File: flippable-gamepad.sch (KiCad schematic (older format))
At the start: 24 parts, among them SW1 SW_Push, U1 ATmega32U4-AU, Y1 16MHz

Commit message: Add ProMicro footprints
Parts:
- added ProMicro1: ProMicro, symbol promicro:ProMicro
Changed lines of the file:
@@
 Text GLabel 8450 3750 1    50   Input ~ 0
 COL1
+$Comp
+L promicro:ProMicro ProMicro1
+U 1 1 616FA80C
+P 6450 1900
+F 0 "ProMicro1" H 6450 2937 60  0000 C CNN
+F 1 "ProMicro" H 6450 2831 60  0000 C CNN
+F 2 "" H 6550 850 60  0000 C CNN
+F 3 "" H 6550 850 60  0000 C CNN
+	1    6450 1900
+	1    0    0    -1
+$EndComp
 $EndSCHEMATC

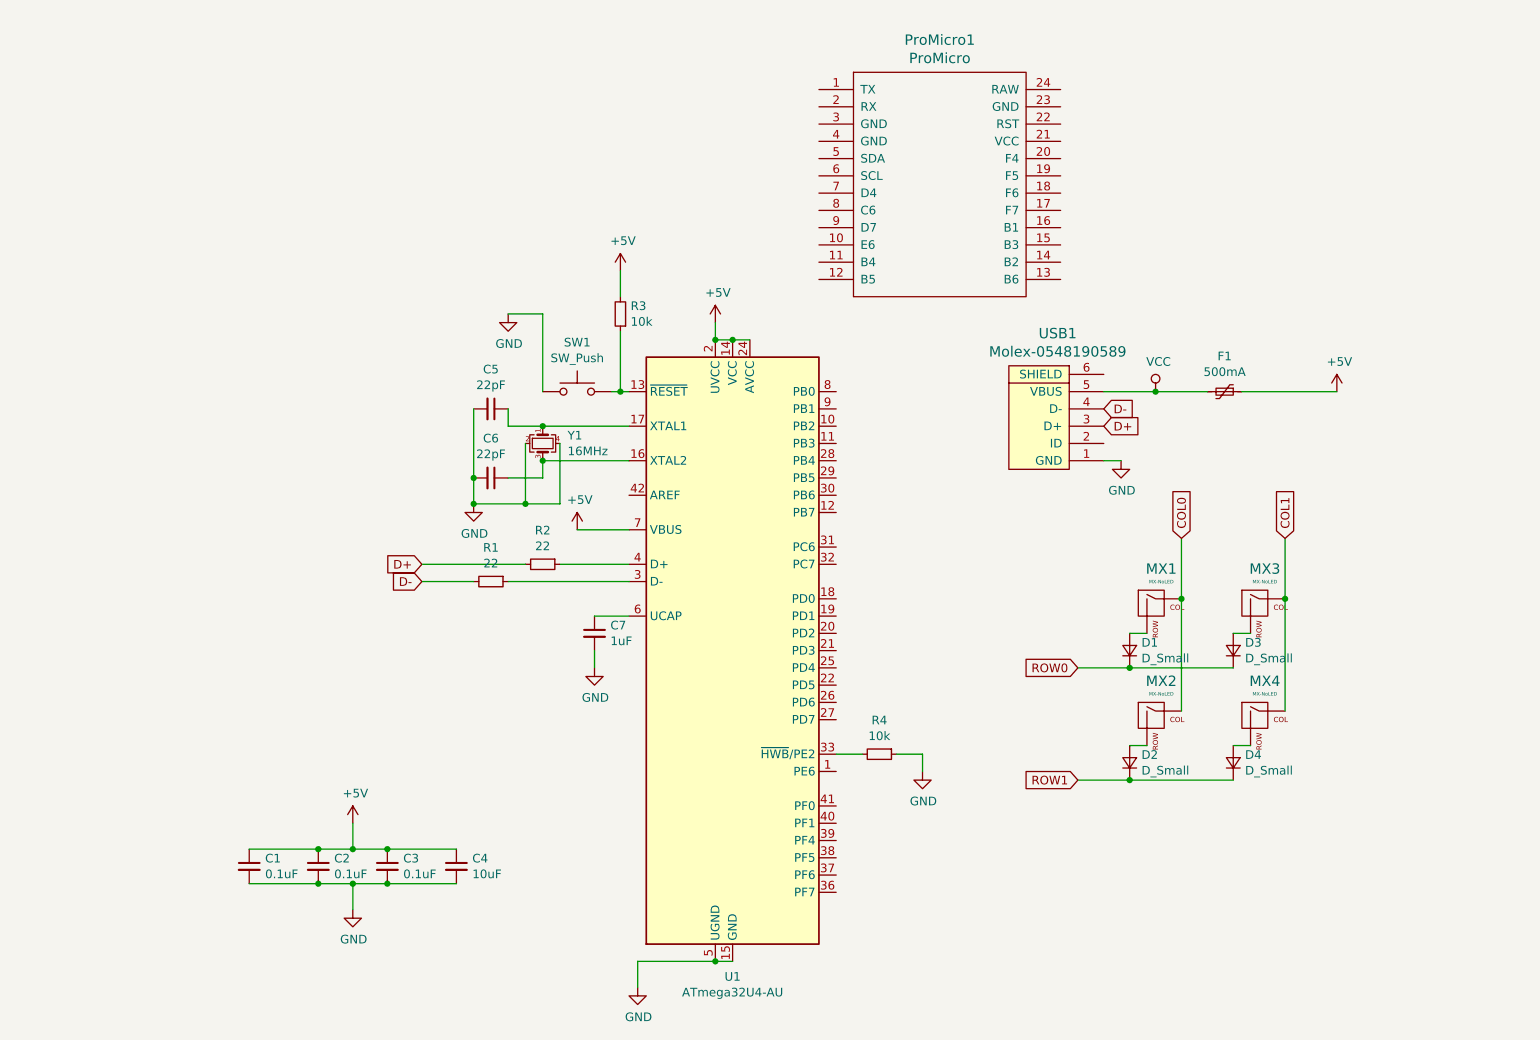
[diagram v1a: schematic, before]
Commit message: Non flippable version test
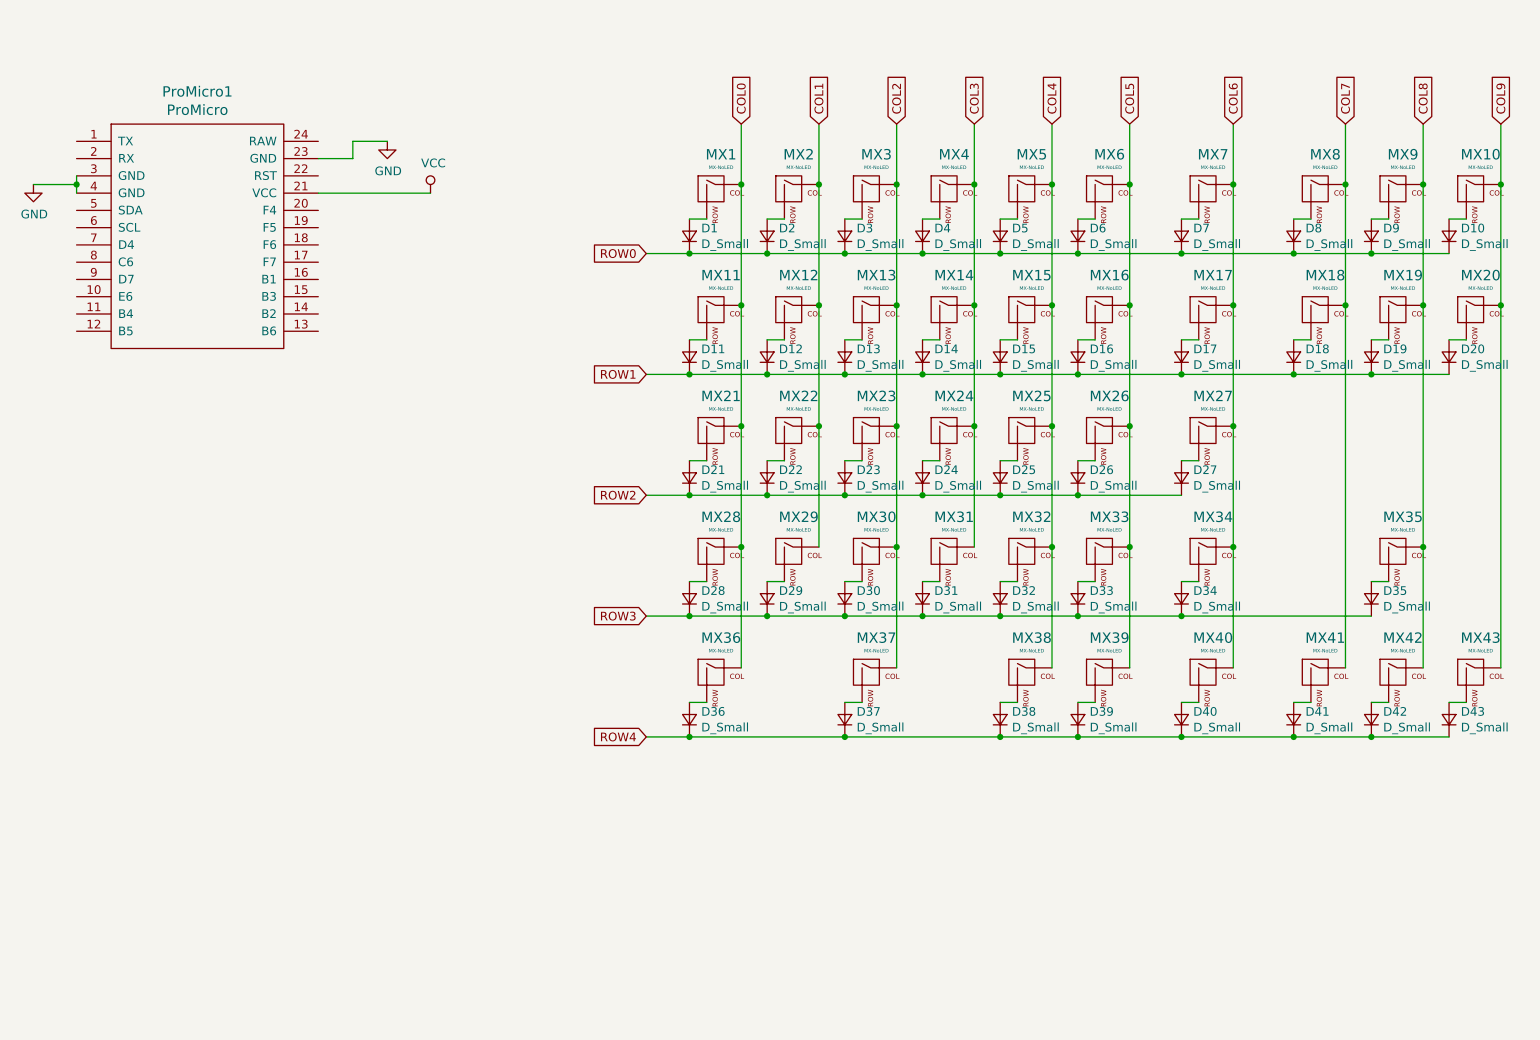
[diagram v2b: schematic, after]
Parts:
- removed C1, C2, C3: 0.1uF, Capacitor_SMD:C_0805_2012Metric, symbol Device:C_Small
- removed C4: 10uF, Capacitor_SMD:C_0805_2012Metric, symbol Device:C_Small
- removed C5, C6: 22pF, Capacitor_SMD:C_0805_2012Metric, symbol Device:C_Small
- removed C7: 1uF, Capacitor_SMD:C_0805_2012Metric, symbol Device:C_Small
- removed F1: 500mA, Fuse:Fuse_1206_3216Metric, symbol Device:Polyfuse_Small
- removed R1, R2: 22, Resistor_SMD:R_0805_2012Metric, symbol Device:R_Small
- removed R3, R4: 10k, Resistor_SMD:R_0805_2012Metric, symbol Device:R_Small
- removed SW1: SW_Push, random-keyboard-parts:SKQG-1155865, symbol Switch:SW_Push
- removed U1: ATmega32U4-AU, Package_QFP:TQFP-44_10x10mm_P0.8mm, symbol MCU_Microchip_ATmega:ATmega32U4-AU
- removed USB1: Molex-0548190589, random-keyboard-parts:Molex-0548190589, symbol random-keyboard-parts:Molex-0548190589
- removed Y1: 16MHz, Crystal:Crystal_SMD_3225-4Pin_3.2x2.5mm, symbol Device:Crystal_GND24_Small
- added D10, D11, D12, D13, D14, D15, D16, D17, D18, D19, D20, D21, D22, D23, D24, D25, D26, D27, D28, D29, D30, D31, D32, D33, D34, D35, D36, D37, D38, D39, D40, D41, D42, D43, D5, D6, D7, D8, D9: D_Small, Diode_SMD:D_SOD-123, symbol Device:D_Small
- added MX10, MX11, MX12, MX13, MX14, MX15, MX16, MX18, MX19, MX20, MX21, MX22, MX23, MX24, MX25, MX26, MX28, MX29, MX30, MX31, MX32, MX33, MX35, MX36, MX38, MX39, MX41, MX42, MX43, MX5, MX6, MX8, MX9: MX-NoLED, MX_Only:MXOnly-1U-NoLED, symbol MX_Alps_Hybrid:MX-NoLED
- added MX17, MX27, MX34, MX40, MX7: MX-NoLED, MX_Only:MXOnly-1.25U-NoLED, symbol MX_Alps_Hybrid:MX-NoLED
- added MX37: MX-NoLED, MX_Only:MXOnly-3U-NoLED, symbol MX_Alps_Hybrid:MX-NoLED
- ProMicro1: footprint (none) -> promicro:ProMicro
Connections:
- net COL0: now also MX11.1 (COL), MX21.1 (COL), MX28.1 (COL), MX36.1 (COL); no longer MX2.1 (COL)
- net COL1: now also MX2.1 (COL), MX12.1 (COL), MX22.1 (COL), MX29.1 (COL); no longer MX3.1 (COL), MX4.1 (COL)
- net GND: now also ProMicro1.23 (GND), ProMicro1.3 (GND), ProMicro1.4 (GND)
- net ROW0: now also D2.1 (K), D4.1 (K), D10.1 (K), D5.1 (K), D6.1 (K), D7.1 (K), D8.1 (K), D9.1 (K)
- net ROW1: now also D11.1 (K), D12.1 (K), D13.1 (K), D14.1 (K), D15.1 (K), D16.1 (K), D17.1 (K), D18.1 (K), D19.1 (K), D20.1 (K); no longer D2.1 (K), D4.1 (K)
- net VCC: now also ProMicro1.21 (VCC)
- new net: D5.2 (A), MX5.2 (ROW)
- new net: D6.2 (A), MX6.2 (ROW)
- new net: D11.2 (A), MX11.2 (ROW)
- new net: D12.2 (A), MX12.2 (ROW)
- new net: D13.2 (A), MX13.2 (ROW)
- new net: D14.2 (A), MX14.2 (ROW)
- new net: D15.2 (A), MX15.2 (ROW)
- new net: D16.2 (A), MX16.2 (ROW)
- new net: D21.2 (A), MX21.2 (ROW)
- new net: D22.2 (A), MX22.2 (ROW)
- new net: D23.2 (A), MX23.2 (ROW)
- new net: D24.2 (A), MX24.2 (ROW)
- new net: D25.2 (A), MX25.2 (ROW)
- new net: D26.2 (A), MX26.2 (ROW)
- new net: D28.2 (A), MX28.2 (ROW)
- new net: D29.2 (A), MX29.2 (ROW)
- new net: D30.2 (A), MX30.2 (ROW)
- new net: D31.2 (A), MX31.2 (ROW)
- new net: D32.2 (A), MX32.2 (ROW)
- new net: D33.2 (A), MX33.2 (ROW)
- new net: D36.2 (A), MX36.2 (ROW)
- new net: D37.2 (A), MX37.2 (ROW)
- new net: D38.2 (A), MX38.2 (ROW)
- new net: D39.2 (A), MX39.2 (ROW)
- new net: D7.2 (A), MX7.2 (ROW)
- new net: D17.2 (A), MX17.2 (ROW)
- new net: D27.2 (A), MX27.2 (ROW)
- new net: D34.2 (A), MX34.2 (ROW)
- new net: D40.2 (A), MX40.2 (ROW)
- new net: D8.2 (A), MX8.2 (ROW)
- new net: D9.2 (A), MX9.2 (ROW)
- new net: D10.2 (A), MX10.2 (ROW)
- new net: D18.2 (A), MX18.2 (ROW)
- new net: D19.2 (A), MX19.2 (ROW)
- new net: D20.2 (A), MX20.2 (ROW)
- new net: D35.2 (A), MX35.2 (ROW)
- new net: D41.2 (A), MX41.2 (ROW)
- new net: D42.2 (A), MX42.2 (ROW)
- new net: D43.2 (A), MX43.2 (ROW)
- new net COL2: MX13.1 (COL), MX23.1 (COL), MX3.1 (COL), MX30.1 (COL), MX37.1 (COL)
- new net COL3: MX14.1 (COL), MX24.1 (COL), MX31.1 (COL), MX4.1 (COL)
- new net COL4: MX15.1 (COL), MX25.1 (COL), MX32.1 (COL), MX38.1 (COL), MX5.1 (COL)
- new net COL5: MX16.1 (COL), MX26.1 (COL), MX33.1 (COL), MX39.1 (COL), MX6.1 (COL)
- new net COL6: MX17.1 (COL), MX27.1 (COL), MX34.1 (COL), MX40.1 (COL), MX7.1 (COL)
- new net COL7: MX18.1 (COL), MX41.1 (COL), MX8.1 (COL)
- new net COL8: MX19.1 (COL), MX35.1 (COL), MX42.1 (COL), MX9.1 (COL)
- new net COL9: MX10.1 (COL), MX20.1 (COL), MX43.1 (COL)
- new net ROW2: D21.1 (K), D22.1 (K), D23.1 (K), D24.1 (K), D25.1 (K), D26.1 (K), D27.1 (K)
- new net ROW3: D28.1 (K), D29.1 (K), D30.1 (K), D31.1 (K), D32.1 (K), D33.1 (K), D34.1 (K), D35.1 (K)
- new net ROW4: D36.1 (K), D37.1 (K), D38.1 (K), D39.1 (K), D40.1 (K), D41.1 (K), D42.1 (K), D43.1 (K)
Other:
- moved on the sheet: ProMicro1

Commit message: Fresh start
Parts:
- removed D15, D37, D38, D39, D40, D41, D42, D43: D_Small, Diode_SMD:D_SOD-123, symbol Device:D_Small
- removed MX15, MX38, MX39, MX41, MX42, MX43: MX-NoLED, MX_Only:MXOnly-1U-NoLED, symbol MX_Alps_Hybrid:MX-NoLED
- removed MX37: MX-NoLED, MX_Only:MXOnly-3U-NoLED, symbol MX_Alps_Hybrid:MX-NoLED
- removed MX40: MX-NoLED, MX_Only:MXOnly-1.25U-NoLED, symbol MX_Alps_Hybrid:MX-NoLED
- added D1: D_Small, Diode_THT:D_DO-35_SOD27_P7.62mm_Horizontal, symbol Device:D_Small
- added MX1: MX-NoLED, MX_Only:MXOnly-1.25U-Reversible-NoLED, symbol MX_Alps_Hybrid:MX-NoLED
- D10, D11, D12, D13, D14, D16, D17, D18, D19, D2, D20, D21, D22, D23, D24, D25, D26, D27, D28, D29, D3, D30, D31, D32, D33, D34, D35, D36, D4, D5, D6, D7, D8, D9: footprint Diode_SMD:D_SOD-123 -> Diode_THT:D_DO-35_SOD27_P7.62mm_Horizontal
- D15: renamed from D1; footprint Diode_SMD:D_SOD-123 -> Diode_THT:D_DO-35_SOD27_P7.62mm_Horizontal
- MX10, MX11, MX12, MX13, MX14, MX18, MX19, MX2, MX20, MX21, MX22, MX23, MX25, MX26, MX28, MX29, MX3, MX30, MX31, MX33, MX36, MX4, MX5, MX6, MX9: footprint MX_Only:MXOnly-1U-NoLED -> MX_Only:MXOnly-1U-Reversible-NoLED
- MX15: renamed from MX1; footprint MX_Only:MXOnly-1U-NoLED -> MX_Only:MXOnly-1U-Reversible-NoLED
- MX16, MX24, MX32, MX8: footprint MX_Only:MXOnly-1U-NoLED -> MX_Only:MXOnly-1.25U-Reversible-NoLED
- MX17, MX27, MX34, MX7: footprint MX_Only:MXOnly-1.25U-NoLED -> MX_Only:MXOnly-1U-Reversible-NoLED
- MX35: footprint MX_Only:MXOnly-1U-NoLED -> MX_Only:MXOnly-3U-Reversible-ReversedStabilizers-NoLED
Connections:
- net COL0: now also MX23.1 (COL), MX31.1 (COL), ProMicro1.13 (B6); no longer MX11.1 (COL), MX21.1 (COL), MX28.1 (COL), MX36.1 (COL)
- net COL1: now also MX16.1 (COL), MX24.1 (COL), MX32.1 (COL), MX8.1 (COL), ProMicro1.14 (B2), MX1.1 (COL); no longer MX12.1 (COL), MX2.1 (COL), MX22.1 (COL), MX29.1 (COL)
- net COL2: now also MX17.1 (COL), MX2.1 (COL), MX25.1 (COL), MX33.1 (COL), MX9.1 (COL), ProMicro1.15 (B3); no longer MX13.1 (COL), MX23.1 (COL), MX3.1 (COL), MX30.1 (COL)
- net COL3: now also MX10.1 (COL), MX18.1 (COL), MX26.1 (COL), MX3.1 (COL), MX34.1 (COL), ProMicro1.16 (B1); no longer MX14.1 (COL), MX24.1 (COL), MX31.1 (COL), MX4.1 (COL)
- net COL4: now also MX11.1 (COL), MX19.1 (COL), MX27.1 (COL), MX4.1 (COL), ProMicro1.17 (F7); no longer MX25.1 (COL), MX32.1 (COL), MX5.1 (COL)
- net COL5: now also MX12.1 (COL), MX20.1 (COL), MX28.1 (COL), MX35.1 (COL), MX5.1 (COL), ProMicro1.18 (F6); no longer MX16.1 (COL), MX26.1 (COL), MX33.1 (COL), MX6.1 (COL)
- net COL6: now also MX13.1 (COL), MX21.1 (COL), MX29.1 (COL), MX6.1 (COL), ProMicro1.19 (F5); no longer MX17.1 (COL), MX27.1 (COL), MX34.1 (COL), MX7.1 (COL)
- net COL7: now also MX14.1 (COL), MX22.1 (COL), MX30.1 (COL), MX36.1 (COL), MX7.1 (COL), ProMicro1.20 (F4); no longer MX18.1 (COL), MX8.1 (COL)
- net ROW0: now also ProMicro1.12 (B5), D1.1 (K); no longer D10.1 (K), D15.1 (K), D8.1 (K), D9.1 (K)
- net ROW1: now also D10.1 (K), D8.1 (K), D9.1 (K), ProMicro1.11 (B4); no longer D16.1 (K), D17.1 (K), D18.1 (K), D19.1 (K), D20.1 (K)
- net ROW2: now also D15.1 (K), D16.1 (K), D17.1 (K), D18.1 (K), D19.1 (K), D20.1 (K), ProMicro1.10 (E6); no longer D23.1 (K), D24.1 (K), D25.1 (K), D26.1 (K), D27.1 (K)
- net ROW3: now also D23.1 (K), D24.1 (K), D25.1 (K), D26.1 (K), D27.1 (K), ProMicro1.9 (D7); no longer D31.1 (K), D32.1 (K), D33.1 (K), D34.1 (K), D35.1 (K)
- net ROW4: now also D31.1 (K), D32.1 (K), D33.1 (K), D34.1 (K), D35.1 (K), ProMicro1.8 (C6)
- removed net COL8: MX19.1 (COL), MX35.1 (COL), MX9.1 (COL)
- removed net COL9: MX10.1 (COL), MX20.1 (COL)
- new net: D1.2 (A), MX1.2 (ROW)
- no-connect marks 0 -> 1
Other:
- moved on the sheet: D15, MX15
